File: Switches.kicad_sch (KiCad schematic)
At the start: 37 parts, among them SW1 SW_SPST, SW10 SW_SPST, SW11 SW_SPST, SW12 SW_SPST, SW15 Rotary, SW16 SW_SPST, SW17 SW_SPST, SW18 SW_SPST, SW19 SW_SPST, SW2 SW_SPST, SW20 Rotary, SW3 SW_SPST, SW4 SW_SPST, SW5 SW_SPST, SW6 SW_SPST, SW7 SW_SPST, SW8 SW_SPST, SW9 SW_SPST

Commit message: Add stm crystal, update title block, add power on LED for 3V3 line
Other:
- company: (none) -> MadMan
- title: (none) -> Crumb Catcher
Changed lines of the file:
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@@
 (kicad_sch (version 20230121) (generator eeschema)
   (paper "A4")
+  (title_block
+    (title "Crumb Catcher")
+    (date "2023-10-25")
+    (rev "A")
+    (company "MadMan")
+  )
   (junction (at 127.635 67.945) (diameter 0) (color 0 0 0 0)
   )

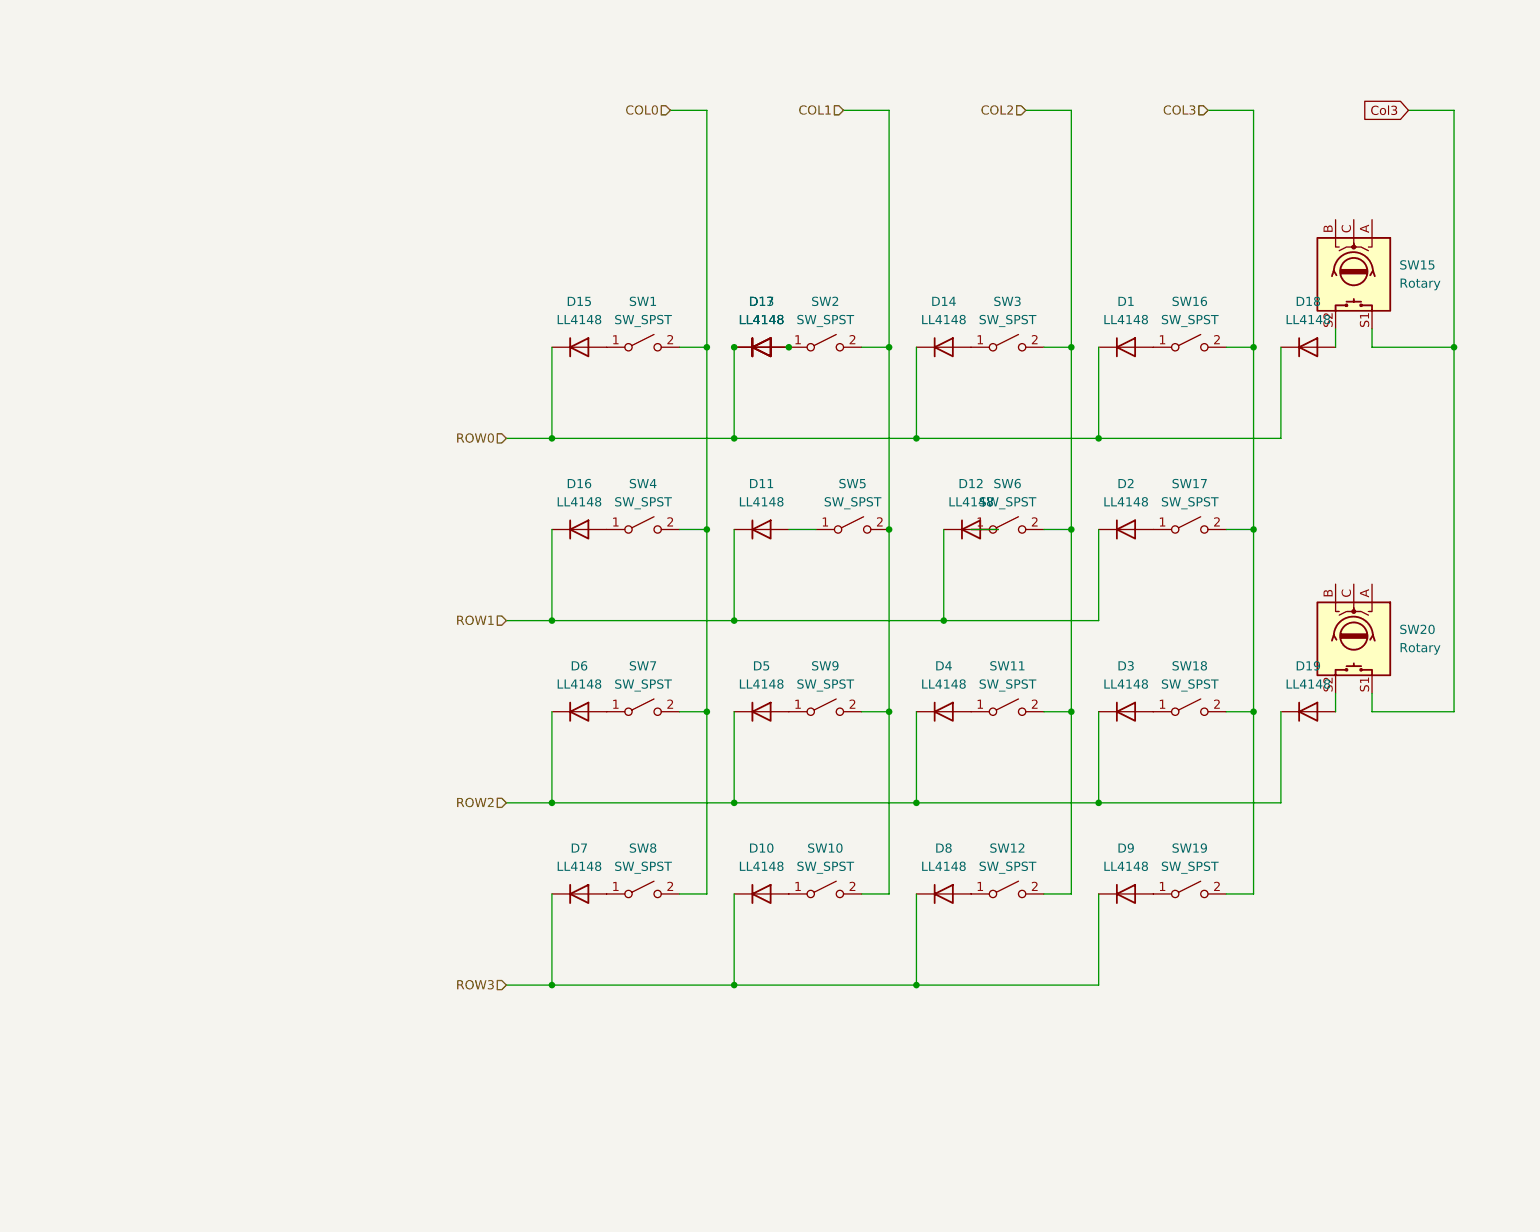
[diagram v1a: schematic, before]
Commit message: Cleanup, Add usb emc and esd
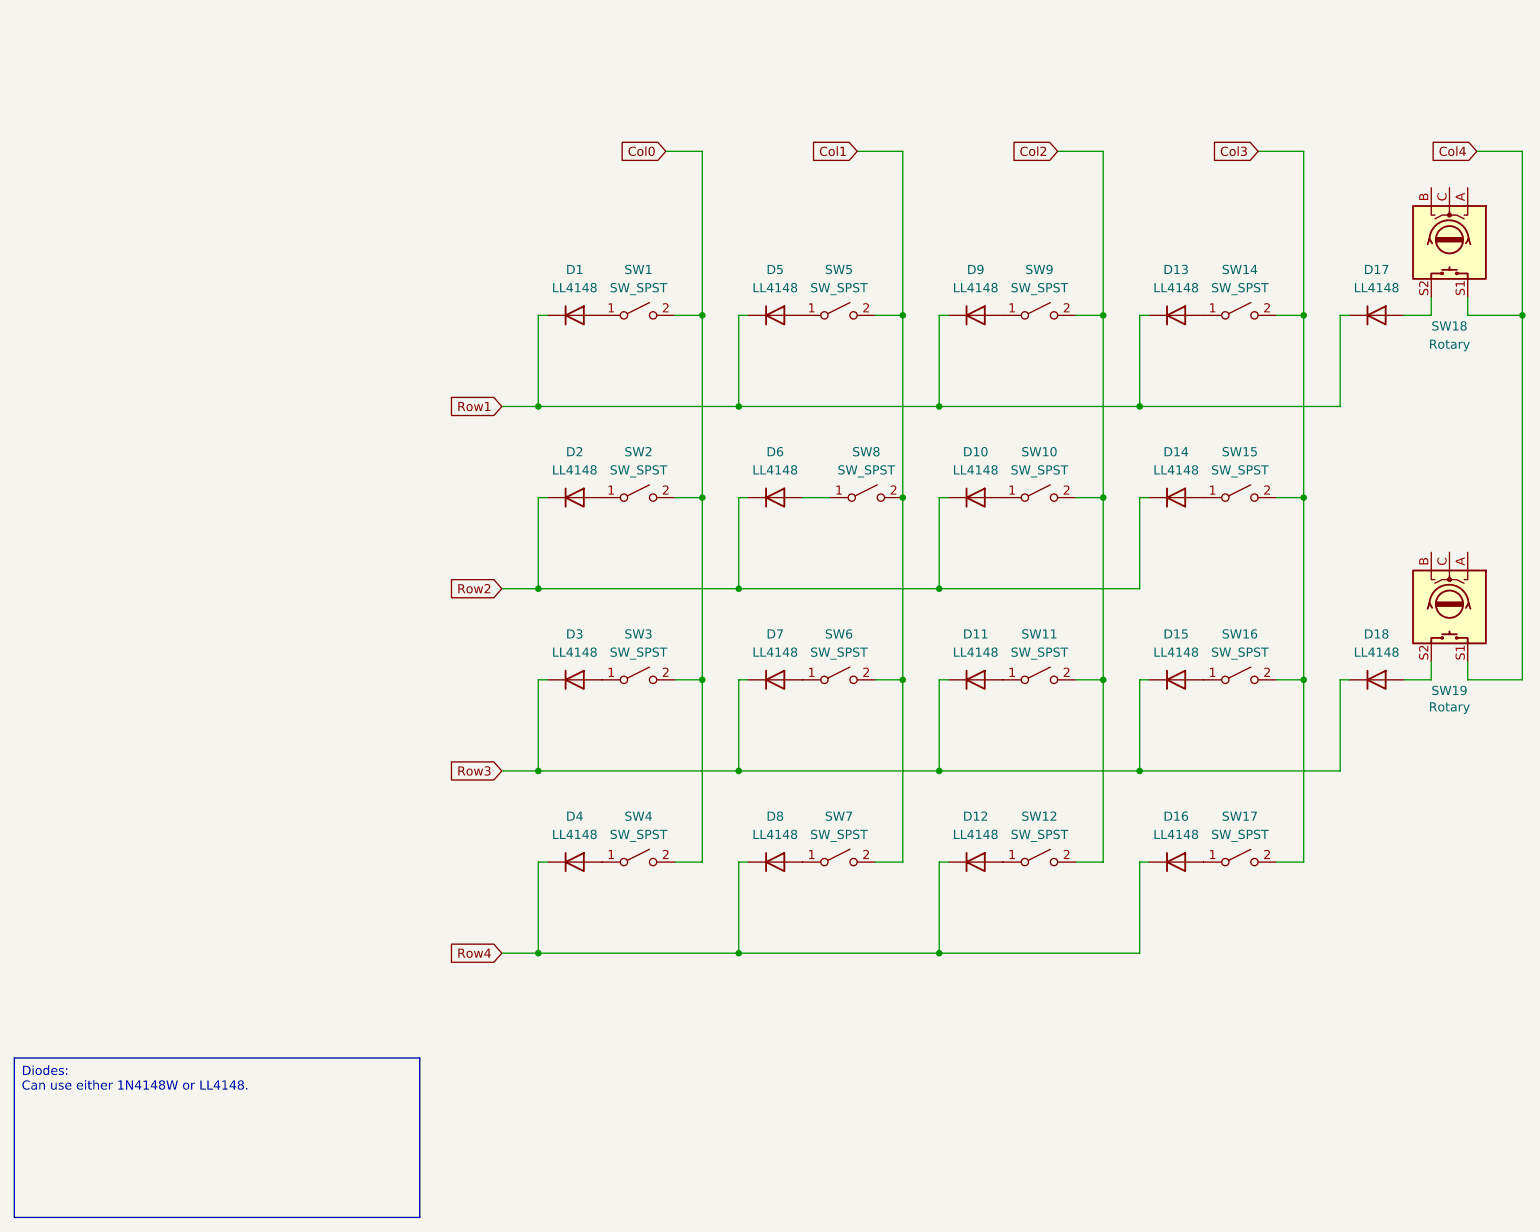
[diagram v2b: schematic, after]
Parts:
- removed D19: LL4148, Diode_SMD:D_MiniMELF, symbol Diode:LL4148
- removed SW15, SW20: Rotary, symbol Device:RotaryEncoder_Switch
- removed SW18, SW19: SW_SPST, PCM_Switch_Keyboard_Cherry_MX:SW_Cherry_MX_PCB_1.00u, symbol Switch:SW_SPST
- added SW14, SW15: SW_SPST, PCM_Switch_Keyboard_Cherry_MX:SW_Cherry_MX_PCB_1.00u, symbol Switch:SW_SPST
- added SW18, SW19: Rotary, symbol Device:RotaryEncoder_Switch
- D1, D10, D11, D12, D13, D14, D15, D16, D17, D18, D2, D3, D4, D5, D6, D7, D8, D9: MPN (none) -> LL4148; Manufacturer (none) -> onsemi; Price (none) -> $0.18; Rating (none) -> DIODE GEN PURP 100V 200MA SOD80; Supplier (none) -> Digikey; Supplier PN (none) -> LL4148FSCT-ND
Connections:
- net COL3 is gone; now on net Col3: SW16.2 (B), SW17.2 (B)
- net Col3: now also SW14.2 (B), SW15.2 (B)
- net at D1.2 (A): now also SW1.1 (A); no longer SW16.1 (A)
- net at D15.2 (A): now also SW16.1 (A); no longer SW1.1 (A)
- net at D2.2 (A): now also SW2.1 (A); no longer SW17.1 (A)
- net at D14.2 (A): now also SW15.1 (A); no longer SW3.1 (A)
- net at D9.2 (A): now also SW9.1 (A)
- net at SW5.1 (A): now also D5.2 (A); no longer D11.2 (A)
- net at D7.2 (A): now also SW6.1 (A); no longer SW8.1 (A)
- net at D3.2 (A): now also SW3.1 (A)
- net at D18.2 (A): now also SW19.S2
- net at D16.2 (A): now also SW17.1 (A); no longer SW4.1 (A)
- net at SW12.1 (A): now also D12.2 (A); no longer D8.2 (A)
- net at SW7.1 (A): now also D8.2 (A); no longer D6.2 (A)
- net at SW11.1 (A): now also D11.2 (A); no longer D4.2 (A)
- net COL0 renamed Col0
- net Col0: now also SW2.2 (B), SW3.2 (B); no longer SW7.2 (B), SW8.2 (B)
- net COL1 renamed Col2
- net Col2: now also SW11.2 (B), SW12.2 (B); no longer SW2.2 (B), SW5.2 (B)
- removed net COL2: SW11.2 (B), SW12.2 (B), SW3.2 (B), SW6.2 (B)
- net ROW0 renamed Row1
- net Row1: now also D5.1 (K), D9.1 (K); no longer D14.1 (K), D15.1 (K), D18.1 (K)
- net ROW1 renamed Row4
- net Row4: now also D4.1 (K), D8.1 (K); no longer D11.1 (K), D2.1 (K)
- removed net ROW2: D3.1 (K), D4.1 (K), D5.1 (K), D6.1 (K)
- removed net ROW3: D10.1 (K), D7.1 (K), D8.1 (K), D9.1 (K)
- new net: D17.2 (A), SW18.S2
- new net: D13.2 (A), SW14.1 (A)
- new net: D6.2 (A), SW8.1 (A)
- new net: D4.2 (A), SW4.1 (A)
- new net Col1: SW5.2 (B), SW6.2 (B), SW7.2 (B), SW8.2 (B)
- new net Col4: SW18.S1, SW19.S1
- new net Row2: D10.1 (K), D14.1 (K), D2.1 (K), D6.1 (K)
- new net Row3: D11.1 (K), D15.1 (K), D18.1 (K), D3.1 (K), D7.1 (K)

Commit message: Start component selection
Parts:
- SW10: renamed from SW9; MPN (none) -> 4958; Manufacturer (none) -> Adafruit Industries LLC; Price (none) -> $0.394; Rating (none) -> KAILH SW SKTS FOR MX-COMP 1=20PC; Supplier (none) -> Digikey; Supplier PN (none) -> 1528-4958-ND
- SW11: renamed from SW10; MPN (none) -> 4958; Manufacturer (none) -> Adafruit Industries LLC; Price (none) -> $0.394; Rating (none) -> KAILH SW SKTS FOR MX-COMP 1=20PC; Supplier (none) -> Digikey; Supplier PN (none) -> 1528-4958-ND
- SW12: renamed from SW11; MPN (none) -> 4958; Manufacturer (none) -> Adafruit Industries LLC; Price (none) -> $0.394; Rating (none) -> KAILH SW SKTS FOR MX-COMP 1=20PC; Supplier (none) -> Digikey; Supplier PN (none) -> 1528-4958-ND
- SW13: renamed from SW12; MPN (none) -> 4958; Manufacturer (none) -> Adafruit Industries LLC; Price (none) -> $0.394; Rating (none) -> KAILH SW SKTS FOR MX-COMP 1=20PC; Supplier (none) -> Digikey; Supplier PN (none) -> 1528-4958-ND
- SW14, SW15, SW16, SW17: MPN (none) -> 4958; Manufacturer (none) -> Adafruit Industries LLC; Price (none) -> $0.394; Rating (none) -> KAILH SW SKTS FOR MX-COMP 1=20PC; Supplier (none) -> Digikey; Supplier PN (none) -> 1528-4958-ND
- SW2: renamed from SW1; MPN (none) -> 4958; Manufacturer (none) -> Adafruit Industries LLC; Price (none) -> $0.394; Rating (none) -> KAILH SW SKTS FOR MX-COMP 1=20PC; Supplier (none) -> Digikey; Supplier PN (none) -> 1528-4958-ND
- SW3: renamed from SW2; MPN (none) -> 4958; Manufacturer (none) -> Adafruit Industries LLC; Price (none) -> $0.394; Rating (none) -> KAILH SW SKTS FOR MX-COMP 1=20PC; Supplier (none) -> Digikey; Supplier PN (none) -> 1528-4958-ND
- SW4: renamed from SW3; MPN (none) -> 4958; Manufacturer (none) -> Adafruit Industries LLC; Price (none) -> $0.394; Rating (none) -> KAILH SW SKTS FOR MX-COMP 1=20PC; Supplier (none) -> Digikey; Supplier PN (none) -> 1528-4958-ND
- SW5: renamed from SW4; MPN (none) -> 4958; Manufacturer (none) -> Adafruit Industries LLC; Price (none) -> $0.394; Rating (none) -> KAILH SW SKTS FOR MX-COMP 1=20PC; Supplier (none) -> Digikey; Supplier PN (none) -> 1528-4958-ND
- SW6: renamed from SW5; MPN (none) -> 4958; Manufacturer (none) -> Adafruit Industries LLC; Price (none) -> $0.394; Rating (none) -> KAILH SW SKTS FOR MX-COMP 1=20PC; Supplier (none) -> Digikey; Supplier PN (none) -> 1528-4958-ND
- SW7: renamed from SW6; MPN (none) -> 4958; Manufacturer (none) -> Adafruit Industries LLC; Price (none) -> $0.394; Rating (none) -> KAILH SW SKTS FOR MX-COMP 1=20PC; Supplier (none) -> Digikey; Supplier PN (none) -> 1528-4958-ND
- SW8: renamed from SW7; MPN (none) -> 4958; Manufacturer (none) -> Adafruit Industries LLC; Price (none) -> $0.394; Rating (none) -> KAILH SW SKTS FOR MX-COMP 1=20PC; Supplier (none) -> Digikey; Supplier PN (none) -> 1528-4958-ND
- SW9: renamed from SW8; MPN (none) -> 4958; Manufacturer (none) -> Adafruit Industries LLC; Price (none) -> $0.394; Rating (none) -> KAILH SW SKTS FOR MX-COMP 1=20PC; Supplier (none) -> Digikey; Supplier PN (none) -> 1528-4958-ND
- renumbered D9 to D10, D10 to D11, D11 to D12, D12 to D13, D13 to D14, D14 to D15, D15 to D16, D16 to D17, D17 to D18, D18 to D19, D1 to D2, D2 to D3, D3 to D4, D4 to D5, D5 to D6, D6 to D7, D7 to D8, D8 to D9
